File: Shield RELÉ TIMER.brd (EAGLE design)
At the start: 160 x 100 mm, 44 parts, among them K1 JS-M1-9V-5, K2 JS-M1-9V-5, K3 JS-M1-9V-5, K4 JS-M1-9V-5, K5 JS-M1-9V-5, K6 JS-M1-9V-5, M1 ARDUINO-NANO-3.0, Q1 BC548, Q2 BC548, Q3 BC548, Q4 BC548, Q5 BC548, Q6 BC548

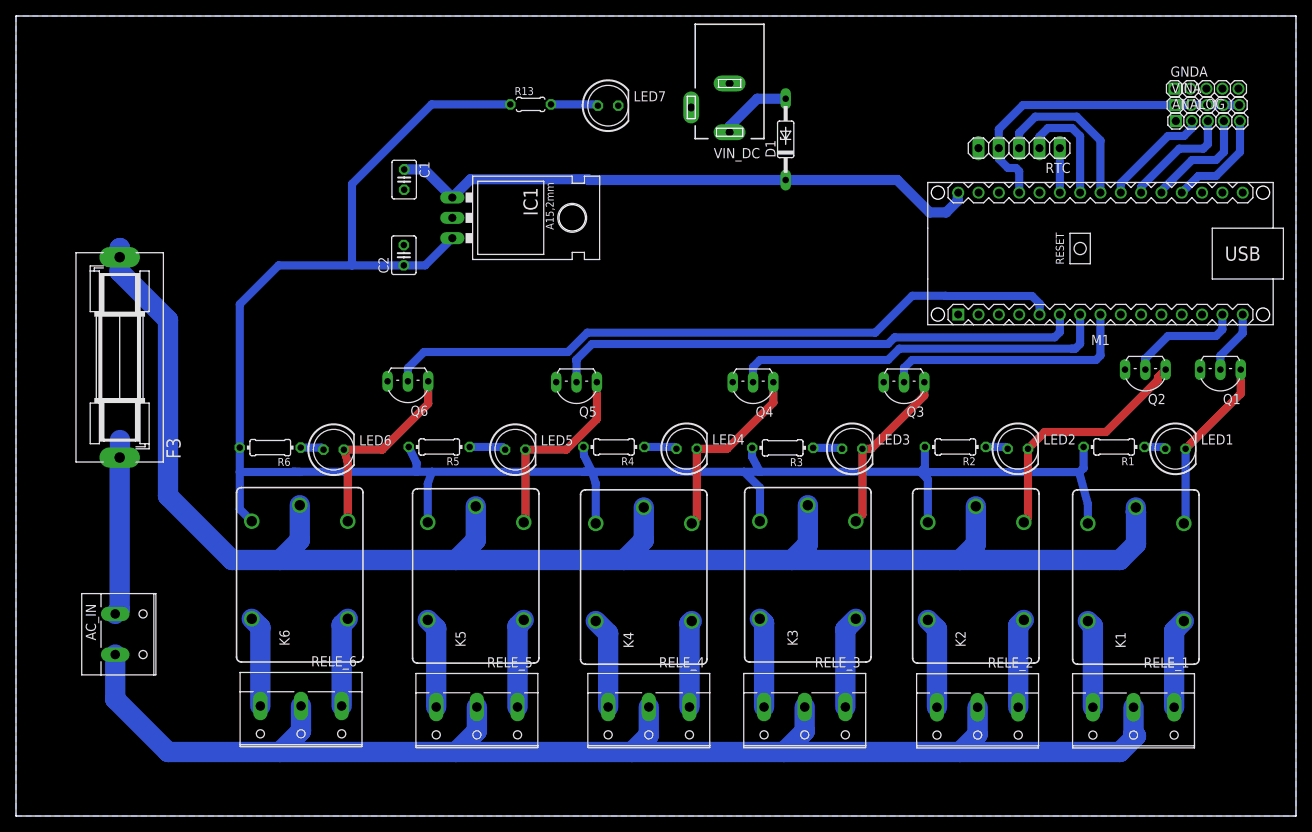
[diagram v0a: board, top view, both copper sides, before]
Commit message: Change-size
Redução de tamanho impresso
Mudança nas vias dos transistor para utilização de JUMPERS
Mudança layout do regulador 7805
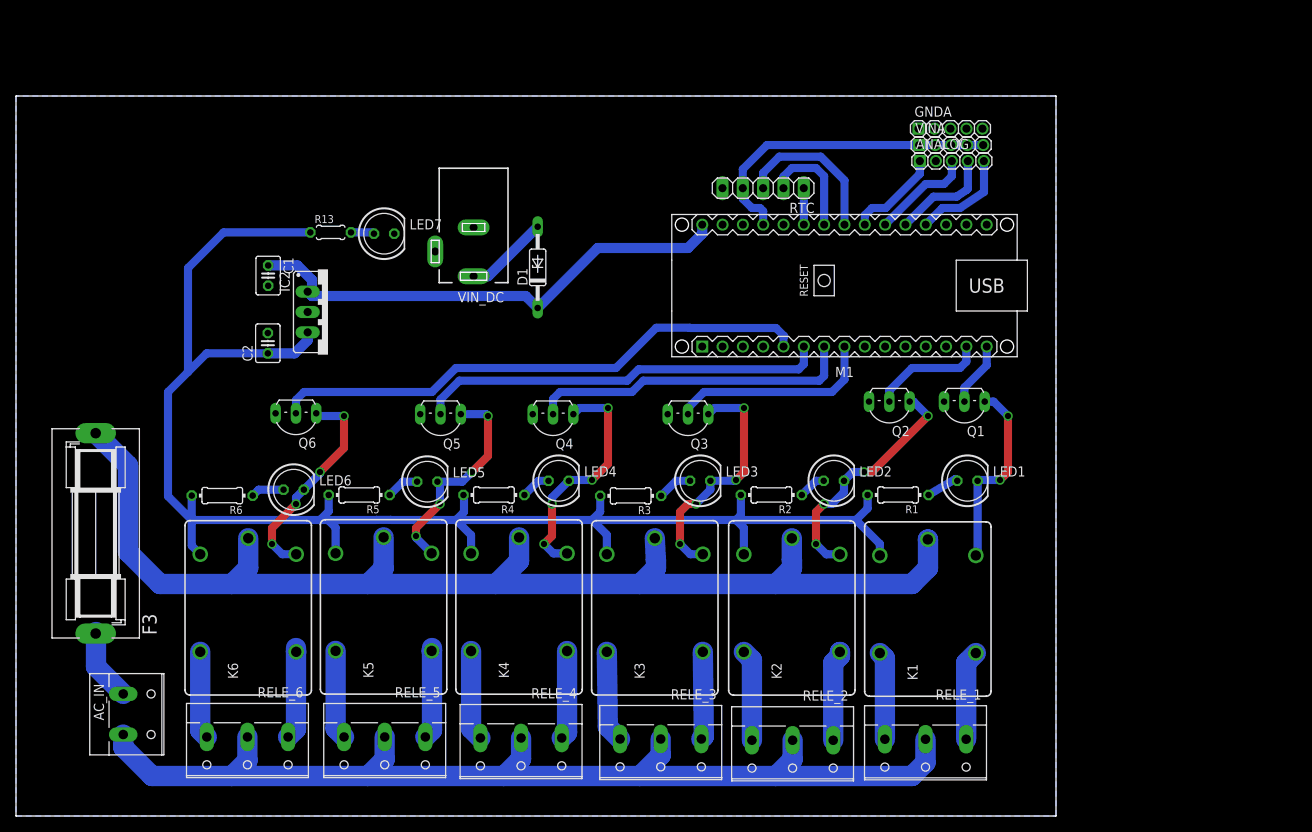
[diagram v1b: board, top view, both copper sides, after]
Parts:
- removed IC1: (no value), v-reg:78XXL
- added IC2: (no value), v-reg:78XXS
- moved VIN_DC 36.7 mm to (57.2, 70.6)
- moved D1 34.9 mm to (65.2, 68.6)
- moved GNDA 32.4 mm to (116.8, 85.9)
- moved ANALOG 32.4 mm to (117.0, 81.9)
- moved RTC 32.4 mm to (93.4, 78.5)
- moved VINA 32.4 mm to (116.9, 83.9)
- moved Q1 32.2 mm to (118.5, 50.5)
- moved LED7 32.2 mm to (46.0, 72.8)
- moved M1 32.2 mm to (103.6, 66.3)
- moved Q2 32.2 mm to (109.2, 50.5)
- moved R13 29.7 mm to (39.3, 73.0)
- moved R1 27.7 mm to (110.3, 40.1)
- moved Q3 27.3 mm to (84.0, 49.0)
- moved LED1 26.3 mm to (118.9, 41.9)
- moved RELE_1 26.3 mm to (113.7, 8.96)
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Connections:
- net +5V: now also IC2.OUT; no longer IC1.OUT
- net A3: now also ANALOG.1; no longer ANALOG.2
- net GND: now also IC2.GND; no longer IC1.GND
- net VIN: now also IC2.IN; no longer IC1.IN
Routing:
- net +5V: track 249.7 -> 201.9 mm
- net PHASE: track 201.6 -> 155.9 mm
- net RETURN: track 173.7 -> 135.0 mm
- net D2: track 86.2 -> 68.5 mm
- net D3: track 66.9 -> 51.3 mm
- net N$16: track 22.0 -> 9.21 mm
- net VIN: track 75.0 -> 63.4 mm
- net N$4: track 21.6 -> 30.9 mm, vias 0 -> 4
- net D4: track 47.7 -> 40.7 mm
- net D5: track 32.1 -> 25.9 mm
- net N$7: track 24.1 -> 30.0 mm, vias 0 -> 4
- net N$19: track 5.94 -> 2.94 mm
- net N$10: track 24.3 -> 27.3 mm, vias 0 -> 4
- net N$35: track 22.2 -> 24.3 mm, vias 0 -> 2
- net N$13: track 24.8 -> 26.9 mm, vias 0 -> 4
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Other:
- board size 160 x 100 mm -> 130 x 90 mm

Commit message: Separete Power to Control
Divisão das trilhas de Alta Potência das trilhas de sinal
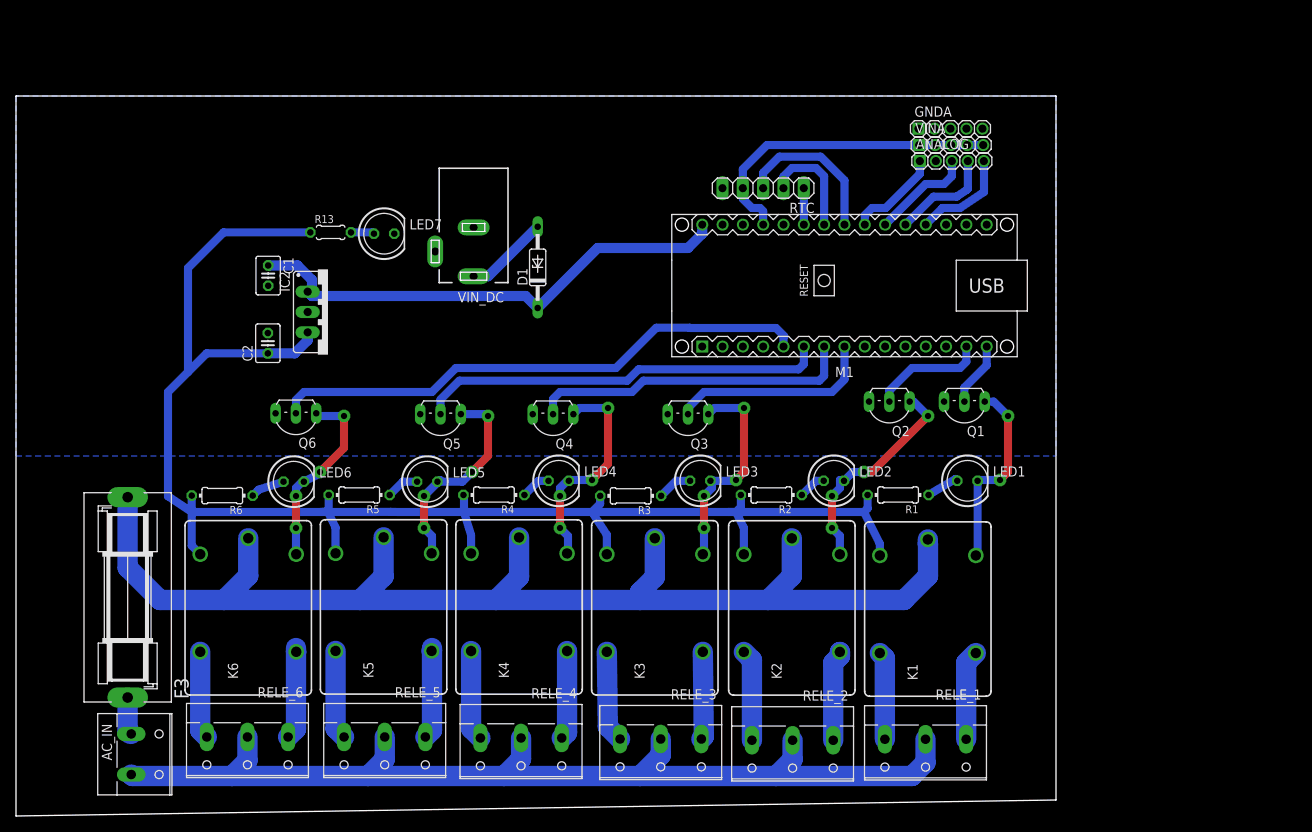
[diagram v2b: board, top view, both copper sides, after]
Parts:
- moved F3 8.94 mm to (14.0, 27.3)
- moved AC_IN 5.10 mm to (15.0, 7.72)
- moved LED6 1.00 mm to (34.7, 41.8)
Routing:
- net PHASE: track 155.9 -> 160.8 mm
- net N$16: track 9.21 -> 4.73 mm
- net RETURN: track 135.0 -> 131.0 mm
- net N$4: track 30.9 -> 27.4 mm
- net N$1: track 30.3 -> 27.5 mm
- net N$13: track 26.9 -> 24.2 mm
- net N$7: track 30.0 -> 27.6 mm
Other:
- outline, holes or cut-outs redrawn
